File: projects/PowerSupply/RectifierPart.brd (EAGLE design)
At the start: 100 x 80 mm, 27 parts, among them K1 G2R2, K2 G2R2, X1 LINE-IN, X2 T1-PRI, X3 T1-SEC, X4 R1-OUT, X5 T2-PRI, X6 T2-SEC, X7 R2-OUT

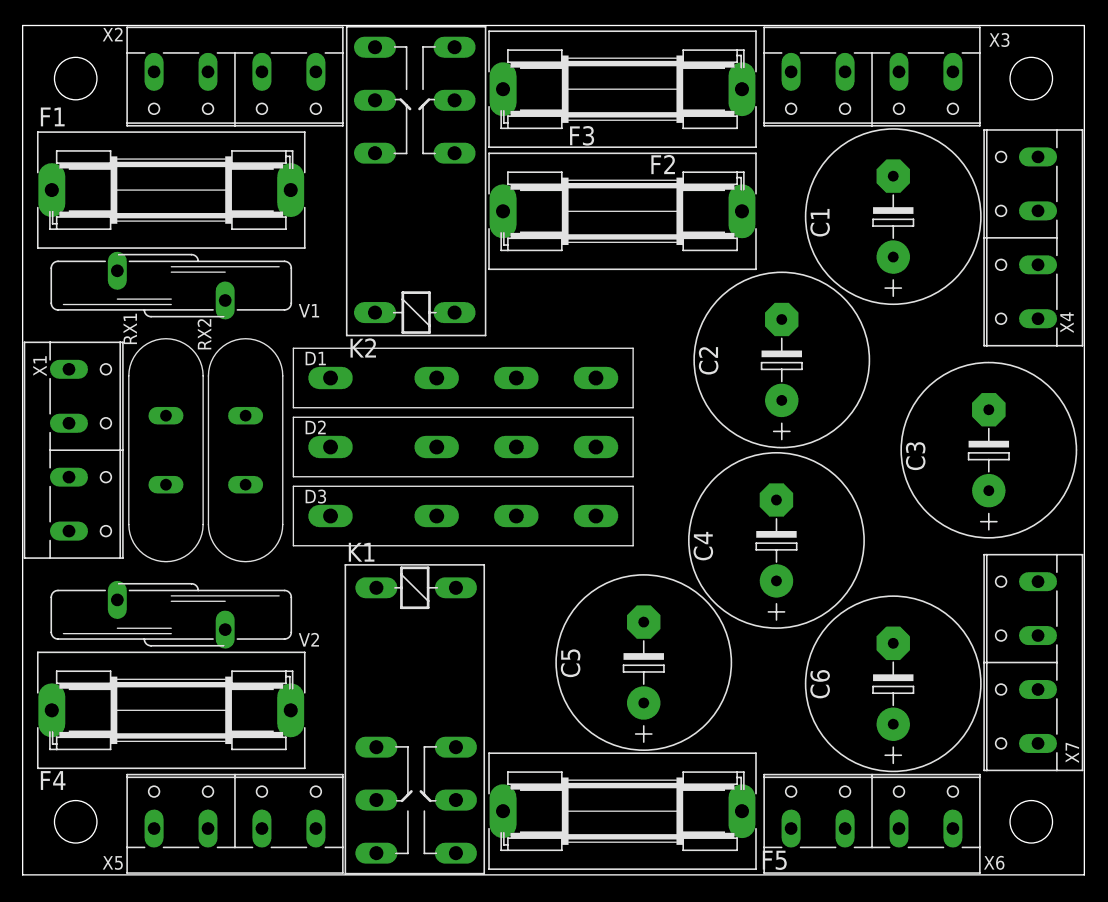
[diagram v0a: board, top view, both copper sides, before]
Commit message: feat: rectifier part modified
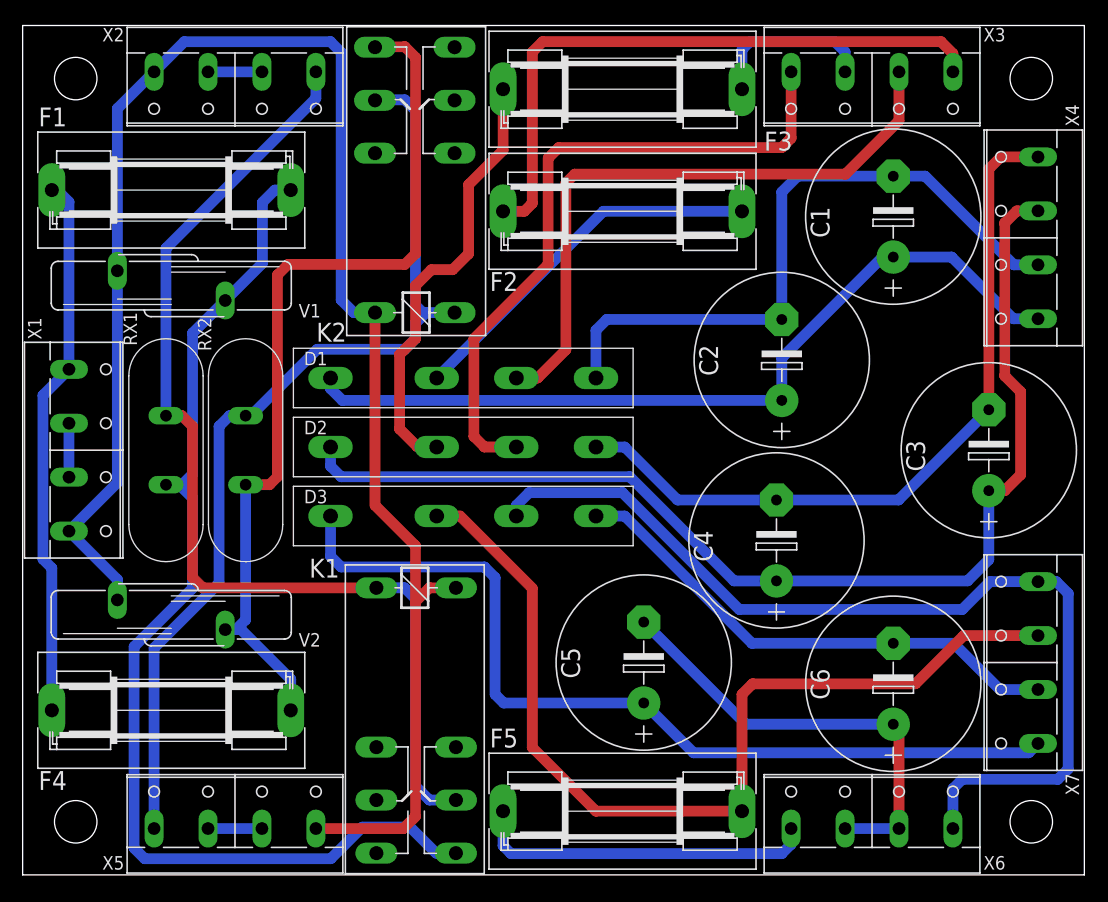
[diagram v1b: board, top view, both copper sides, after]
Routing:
- net -230VAC: track 0.00 -> 164.4 mm
- net N$6: track 0.00 -> 107.2 mm
- net N$3: track 0.00 -> 105.6 mm
- net N$2: track 0.00 -> 99.2 mm
- net N$24: track 0.00 -> 91.8 mm
- net N$19: track 0.00 -> 91.5 mm
- net N$18: track 0.00 -> 90.2 mm
- net N$11: track 0.00 -> 84.9 mm
- net N$20: track 0.00 -> 84.9 mm
- net N$4: track 0.00 -> 78.4 mm
- net N$9: track 0.00 -> 70.4 mm
- net N$15: track 0.00 -> 63.4 mm
- net N$7: track 0.00 -> 62.6 mm
- net N$1: track 0.00 -> 59.9 mm
- net N$8: track 0.00 -> 59.5 mm
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
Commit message: feat: rectifier changes applied
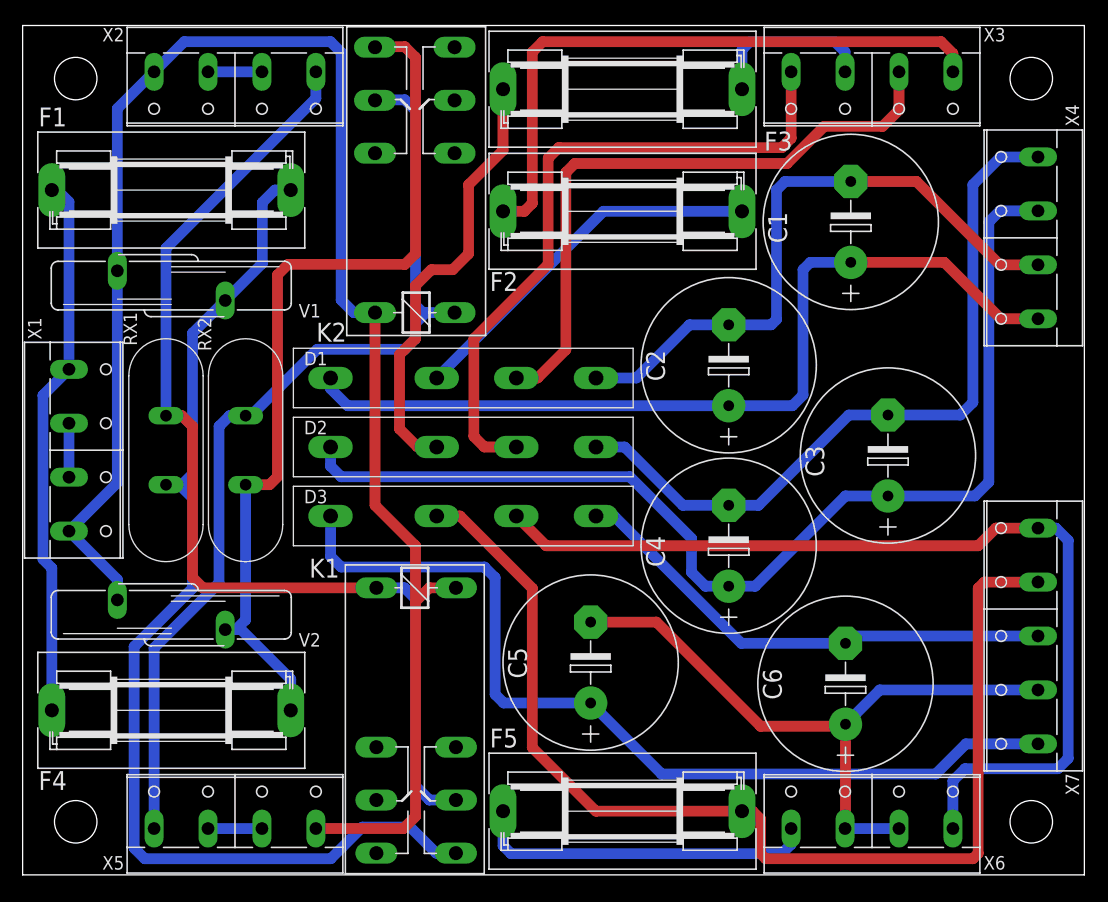
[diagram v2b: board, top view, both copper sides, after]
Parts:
- X7: device con-wago-508:W237-4P -> con-wago-508:W237-5P
- moved C3 9.51 mm to (81.5, 39.5)
- moved C2 5.02 mm to (66.5, 48.0)
- moved C5 5.00 mm to (53.5, 20.0)
- moved C4 4.53 mm to (66.5, 31.0)
- moved C6 4.50 mm to (77.5, 18.0)
- moved C1 4.03 mm to (78.0, 61.5)
- moved X7 2.50 mm to (95.0, 22.5)
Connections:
- net N$18: now also X7.4; no longer X7.3
- net N$19: now also X7.5; no longer X7.4
- net N$21: now also X7.3; no longer X7.2
- net N$22: now also X7.2
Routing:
- net N$22: track 42.6 -> 62.5 mm
- net N$18: track 90.2 -> 106.1 mm
- net N$4: track 78.4 -> 83.0 mm
- net N$6: track 107.2 -> 104.0 mm
- net N$7: track 62.6 -> 59.7 mm
- net N$20: track 84.9 -> 86.5 mm
- net N$21: track 48.4 -> 46.9 mm
- net N$9: track 70.4 -> 69.5 mm
